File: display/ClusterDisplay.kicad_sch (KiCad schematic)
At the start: 88 parts, among them J1 Verdin iMX95 Hexa 8GB WB IT, J10 RTC coin cell, J2 Phoenix MKDS 1,5/3-5,08 power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, J3 Molex KK-254 22-27-2031 CAN (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, J4 TST040HDBC-42 panel, J8 Samtec TSW-108-07-G-S JTAG (b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, J9 Samtec TSW-104-07-G-S buttons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, Q1 PMV55ENEA (AEC-Q101, 60V/20V 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, Q2 PMV55ENEA (AEC-Q101, 60V/20V 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, U1 LM74930-Q1, U2 LM61460-Q1, U3 TLV767-Q1, U4 TCAN1044V-Q1, U6 TPS65131-Q1, U7 TPS61165-Q1

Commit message: display rev B: ignition-wake circuit on the Verdin WAKE1 pin, re-routed
IGN -> 56k -> clamped divider (BAV99-Q to GND/+5V) -> PMV55ENEA pulling
IGN_WAKE_N low, 10k pull-up to +1V8, onto CTRL_WAKE1_MICO# (X1 252). ERC now
0 violations, routed 0 unconnected, BOM regenerated.

Co-Authored-By: Claude Sonnet 5.5 <noreply@anthropic.com>
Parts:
- added C53: 10n ignition filter, Capacitor_SMD:C_0603_1608Metric, symbol ClusterDisplay:C
- added D5: BAV99-Q ignition clamp (AEC-Q101), Package_TO_SOT_SMD:SOT-23, symbol ClusterDisplay:D_BAV99
- added Q3: PMV55ENEA ignition wake pulldown, Package_TO_SOT_SMD:SOT-23, symbol ClusterDisplay:NFET
- added R51: 56k ignition series, Resistor_SMD:R_0603_1608Metric, symbol ClusterDisplay:R
- added R52: 33k ignition divider bottom, Resistor_SMD:R_0603_1608Metric, symbol ClusterDisplay:R
- added R53: 10k wake pull-up to +1V8, Resistor_SMD:R_0603_1608Metric, symbol ClusterDisplay:R
- J3: value Molex KK-254 22-27-2031 CAN (DTM06-3S pigtail) -> Molex KK-254 22-27-2031 private CAN link to gauges/ J8
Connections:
- net +1V8: now also R53.1
- net +5V: now also D5.2 (K2)
- net GND: now also C53.2, D5.1 (A1), Q3.3 (S), R52.2
- net IGN_SENSE: now also R51.1
- net IGN_WAKE_N: now reaches J1.252 (CTRL_WAKE1_MICO#)
- net IGN_WAKE_N: now also Q3.2 (D), R53.2
- new net IGN_GATE: C53.1, D5.3 (CA), Q3.1 (G), R51.2, R52.1
- no-connect marks 200 -> 199

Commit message: Prepare both boards for fabrication: real power-stage values, orderable BOMs, fab packages
display/ power stage was placeholders inherited from fascia-pcb (RILIM, OV top,
RT, FB top...). Values are now calculated from the LM74930-Q1, LM61460-Q1 and
TLV767-Q1 datasheets, with real packages (1u XEL5030 inductor, 1206 caps, 2 mohm
sense resistor, polymer bulk cap). gauges/ buck inductor (XAL5050, Isat above the
LMR33630 current limit) and input/output capacitors fixed per its datasheet.
tools/passive_catalog.py maps every passive to a real MPN (entries flagged
verified or pattern). fab/build_fab.py writes gerbers, drill, CPL and BOM CSVs
and refuses boards with unconnected nets. Silkscreen text raised to the fab
minimum; gauges input zones moved beside the MCU. Both boards re-routed, 0
unconnected.

Co-Authored-By: Claude Sonnet 5.5 <noreply@anthropic.com>
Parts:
- removed C1: 100uF, Capacitor_SMD:C_0603_1608Metric, symbol ClusterDisplay:C
- removed C10: 10u out, Capacitor_SMD:C_0603_1608Metric, symbol ClusterDisplay:C
- removed C5, C9: 10u in, Capacitor_SMD:C_0603_1608Metric, symbol ClusterDisplay:C
- removed C8: 44u out, Capacitor_SMD:C_0603_1608Metric, symbol ClusterDisplay:C
- removed L1: 2.2u, Inductor_SMD:L_1210_3225Metric, symbol ClusterDisplay:L
- removed R1: 2m sense, Resistor_SMD:R_0603_1608Metric, symbol ClusterDisplay:R
- added C1: 100u 35V hybrid polymer hold-up (Panasonic EEH-ZA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, Capacitor_SMD:CP_Elec_8x10, symbol ClusterDisplay:CP_HYBRID
- added C10: 10u COUT, Capacitor_SMD:C_0805_2012Metric, symbol ClusterDisplay:C_0805
- added C5: 4.7u CIN VIN1, Capacitor_SMD:C_1206_3216Metric, symbol ClusterDisplay:C_1206
- added C54, C59, C8: 22u COUT, Capacitor_SMD:C_1206_3216Metric, symbol ClusterDisplay:C_1206
- added C55: 4.7u CIN VIN2, Capacitor_SMD:C_1206_3216Metric, symbol ClusterDisplay:C_1206
- added C56: 100n CHF VIN1, Capacitor_SMD:C_0603_1608Metric, symbol ClusterDisplay:C
- added C57: 100n CHF VIN2, Capacitor_SMD:C_0603_1608Metric, symbol ClusterDisplay:C
- added C58: 22p CFF, Capacitor_SMD:C_0603_1608Metric, symbol ClusterDisplay:C
- added C9: 10u CIN, Capacitor_SMD:C_0805_2012Metric, symbol ClusterDisplay:C_0805
- added L1: 1u XEL5030-102ME 2.1MHz, Inductor_SMD:L_Coilcraft_XAL5030-XXX, symbol ClusterDisplay:L_5030
- added R1: 2m 2% sense (Susumu KRL3216E-C-R002-G-T5), Resistor_SMD:R_1206_3216Metric, symbol ClusterDisplay:R_1206
- C4: value open CT -> 100n CTMR
- C52: value 10u BL output 25V (AEC-Q200) -> 4.7u BL output, 50V part (AEC-Q200)
- R10: value FB top -> 100k FB top
- R11: value FB bot -> 24.9k FB bot
- R12: value RT -> 6.04k RT
- R13: value EN top -> 100k EN top
- R14: value EN bot -> 24.9k EN bot
- R17: value FB top -> 124k FB top
- R18: value FB bot -> 100k FB bot
- R2: value 50R -> 49.9R 1% RSET
- R3: value RILIM -> 60.4k RILIM
- R4: value 5k RMON -> 10k RIMON
- R5: value OV top -> 100k OV top
- R6: value OV bot -> 2.05k OV bot
- R7: value UV top -> 100k UV top
- R8: value UV bot -> 11.5k UV bot
- R9: value RBOOT -> 0R RBOOT
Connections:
- net +12V_PROT: now also C1.1, C5.1, C55.1, C56.1, C57.1
- net +1V8: now also C10.1
- net +5V: now also C54.1, C58.1, C59.1, C8.1, C9.1, L1.2
- net FB_5V: now also C58.2
- net GND: now also C1.2, C10.2, C5.2, C54.2, C55.2, C56.2, C57.2, C59.2, C8.2, C9.2
- net SENSE_OUT: now also R1.2
- net SW_5V: now also L1.1
- net VBAT_F: now also R1.1

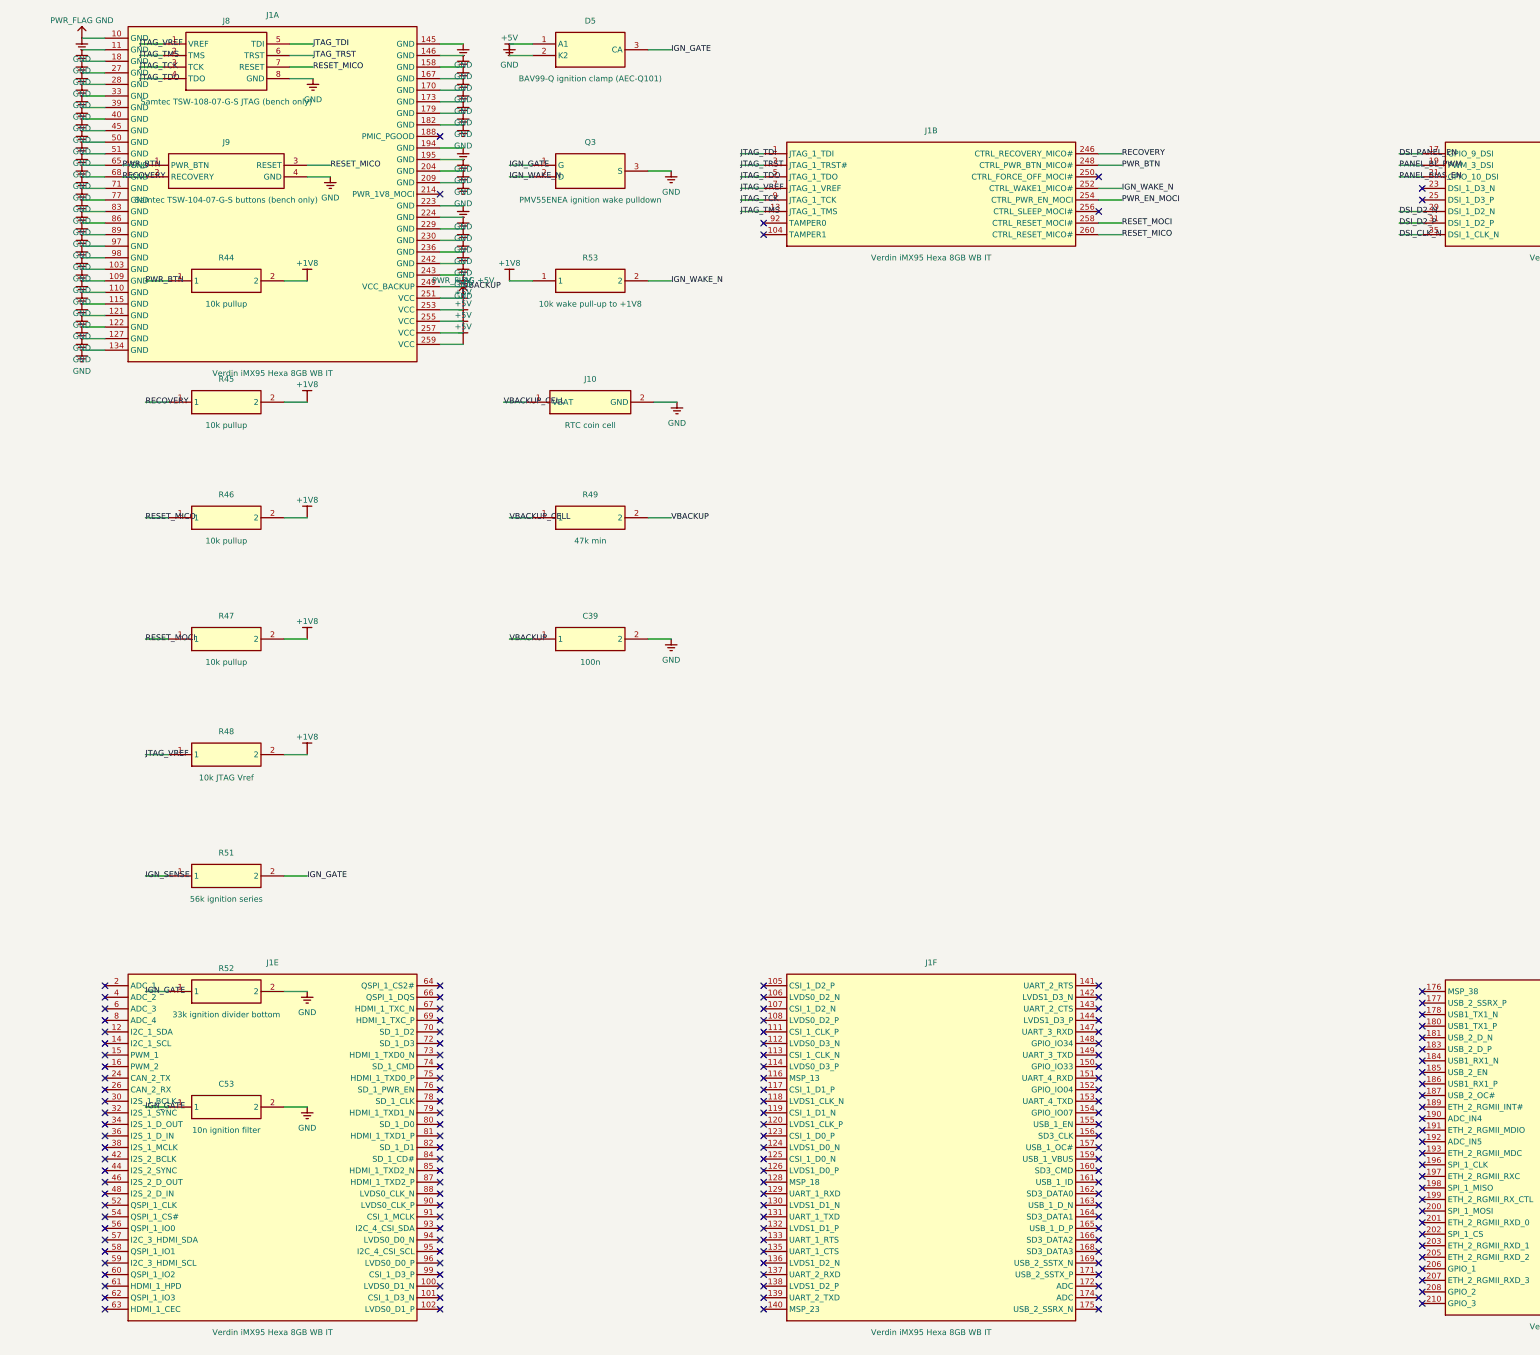
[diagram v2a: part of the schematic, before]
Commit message: display: add rotary dial input (J11): 360-degree pot on Verdin ADC_1 plus click on GPIO_1
KK-254 4-pin connector: filtered 1.8V pot supply, wiper through 1k/100nF to ADC_IN0, click with 10k pull-up and
debounce to GPIO_1, BAV99-Q clamps on both external lines. ERC 0 violations, re-routed 0 unconnected, BOM and fab
package regenerated. The dial itself is a companion line still needing a part choice.

Co-Authored-By: Claude Sonnet 5.5 <noreply@anthropic.com>
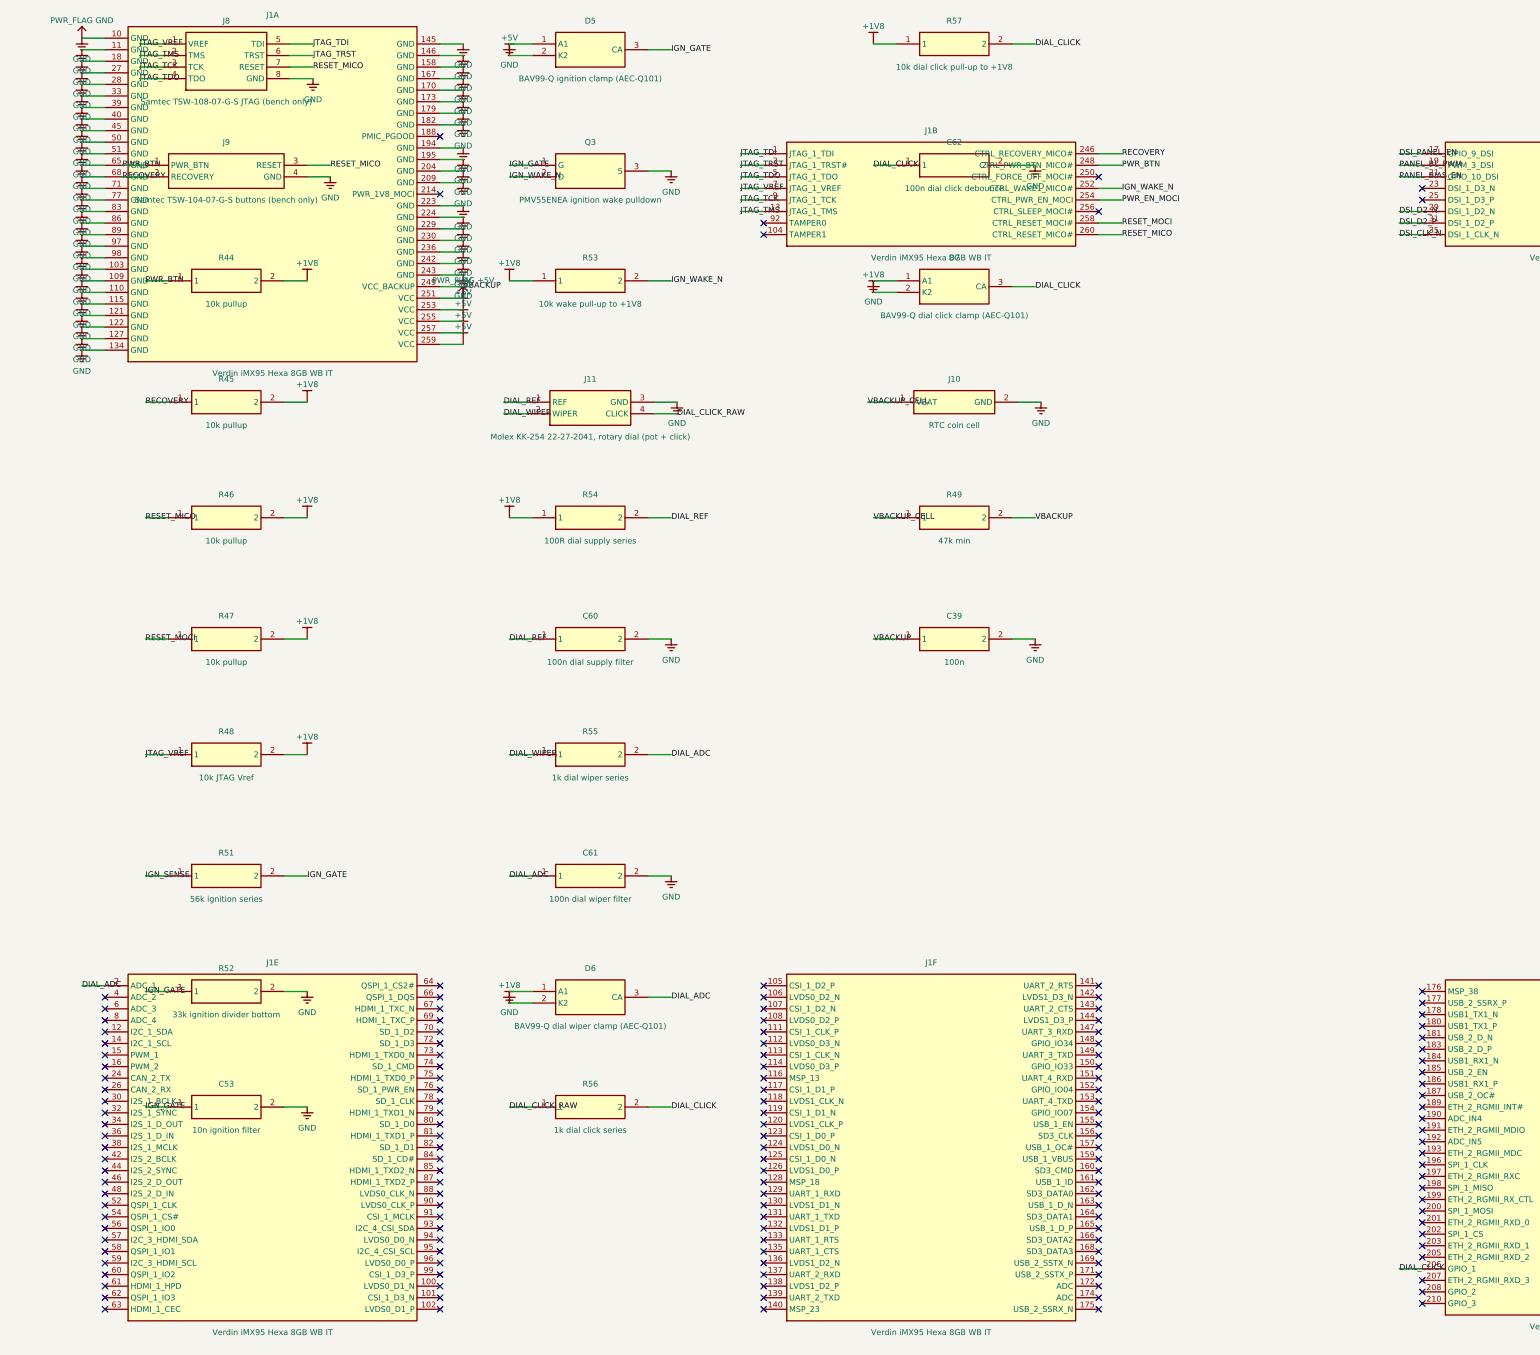
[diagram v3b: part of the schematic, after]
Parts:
- added C60: 100n dial supply filter, Capacitor_SMD:C_0603_1608Metric, symbol ClusterDisplay:C
- added C61: 100n dial wiper filter, Capacitor_SMD:C_0603_1608Metric, symbol ClusterDisplay:C
- added C62: 100n dial click debounce, Capacitor_SMD:C_0603_1608Metric, symbol ClusterDisplay:C
- added D6: BAV99-Q dial wiper clamp (AEC-Q101), Package_TO_SOT_SMD:SOT-23, symbol ClusterDisplay:D_BAV99
- added D7: BAV99-Q dial click clamp (AEC-Q101), Package_TO_SOT_SMD:SOT-23, symbol ClusterDisplay:D_BAV99
- added J11: Molex KK-254 22-27-2041, rotary dial (pot + click), Connector_Molex:Molex_KK-254_AE-6410-04A_1x04_P2.54mm_Vertical, symbol ClusterDisplay:CONN_DIAL
- added R54: 100R dial supply series, Resistor_SMD:R_0603_1608Metric, symbol ClusterDisplay:R
- added R55: 1k dial wiper series, Resistor_SMD:R_0603_1608Metric, symbol ClusterDisplay:R
- added R56: 1k dial click series, Resistor_SMD:R_0603_1608Metric, symbol ClusterDisplay:R
- added R57: 10k dial click pull-up to +1V8, Resistor_SMD:R_0603_1608Metric, symbol ClusterDisplay:R
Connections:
- net +1V8: now also D6.2 (K2), D7.2 (K2), R54.1, R57.1
- net GND: now also C60.2, C61.2, C62.2, D6.1 (A1), D7.1 (A1), J11.3 (GND)
- net DIAL_CLICK: now reaches J1.206 (GPIO_1)
- net DIAL_CLICK: now also C62.1, D7.3 (CA), R56.2, R57.2
- net DIAL_ADC: now reaches J1.2 (ADC_1)
- net DIAL_ADC: now also C61.1, D6.3 (CA), R55.2
- new net DIAL_CLICK_RAW: J11.4 (CLICK), R56.1
- new net DIAL_REF: C60.1, J11.1 (REF), R54.2
- new net DIAL_WIPER: J11.2 (WIPER), R55.1
- no-connect marks 199 -> 197
